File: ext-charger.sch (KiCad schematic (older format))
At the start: 61 parts

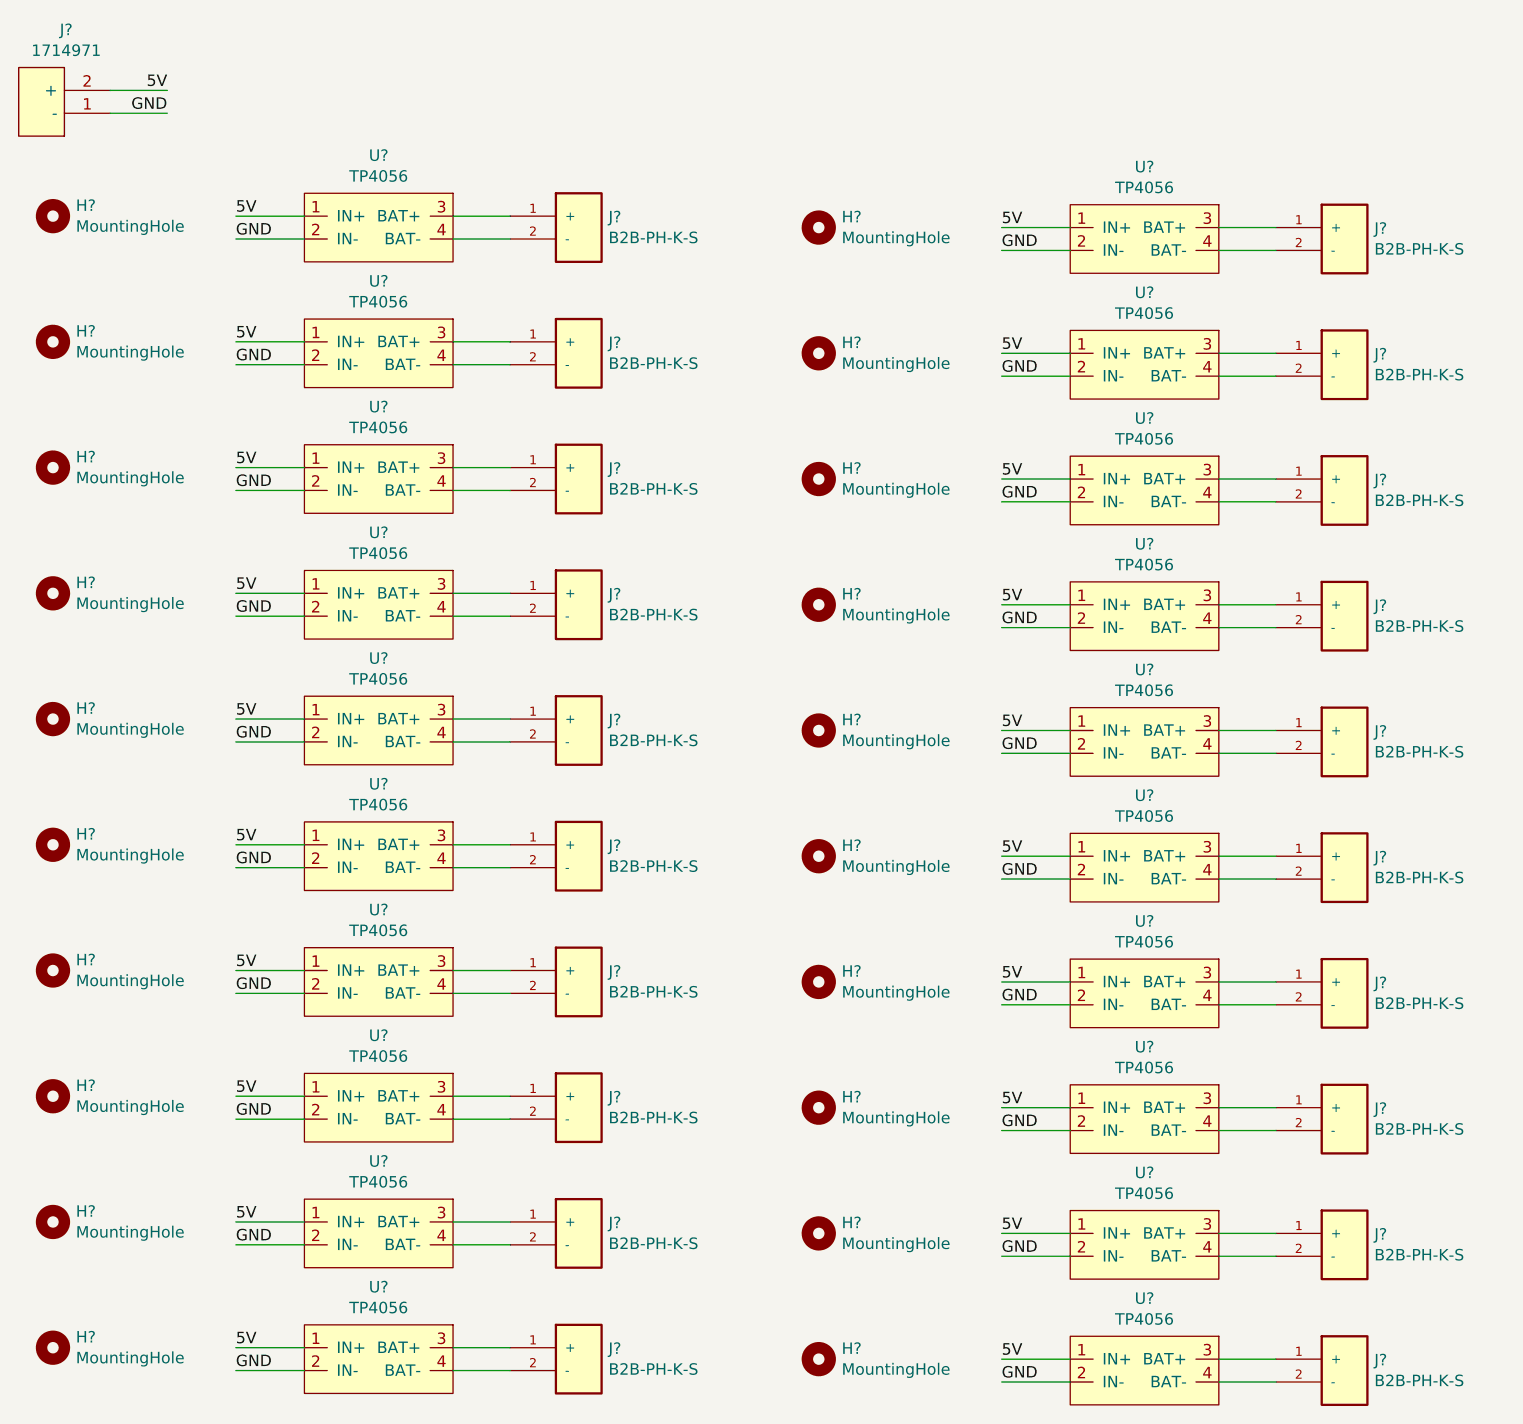
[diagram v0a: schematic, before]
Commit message: added filled zones
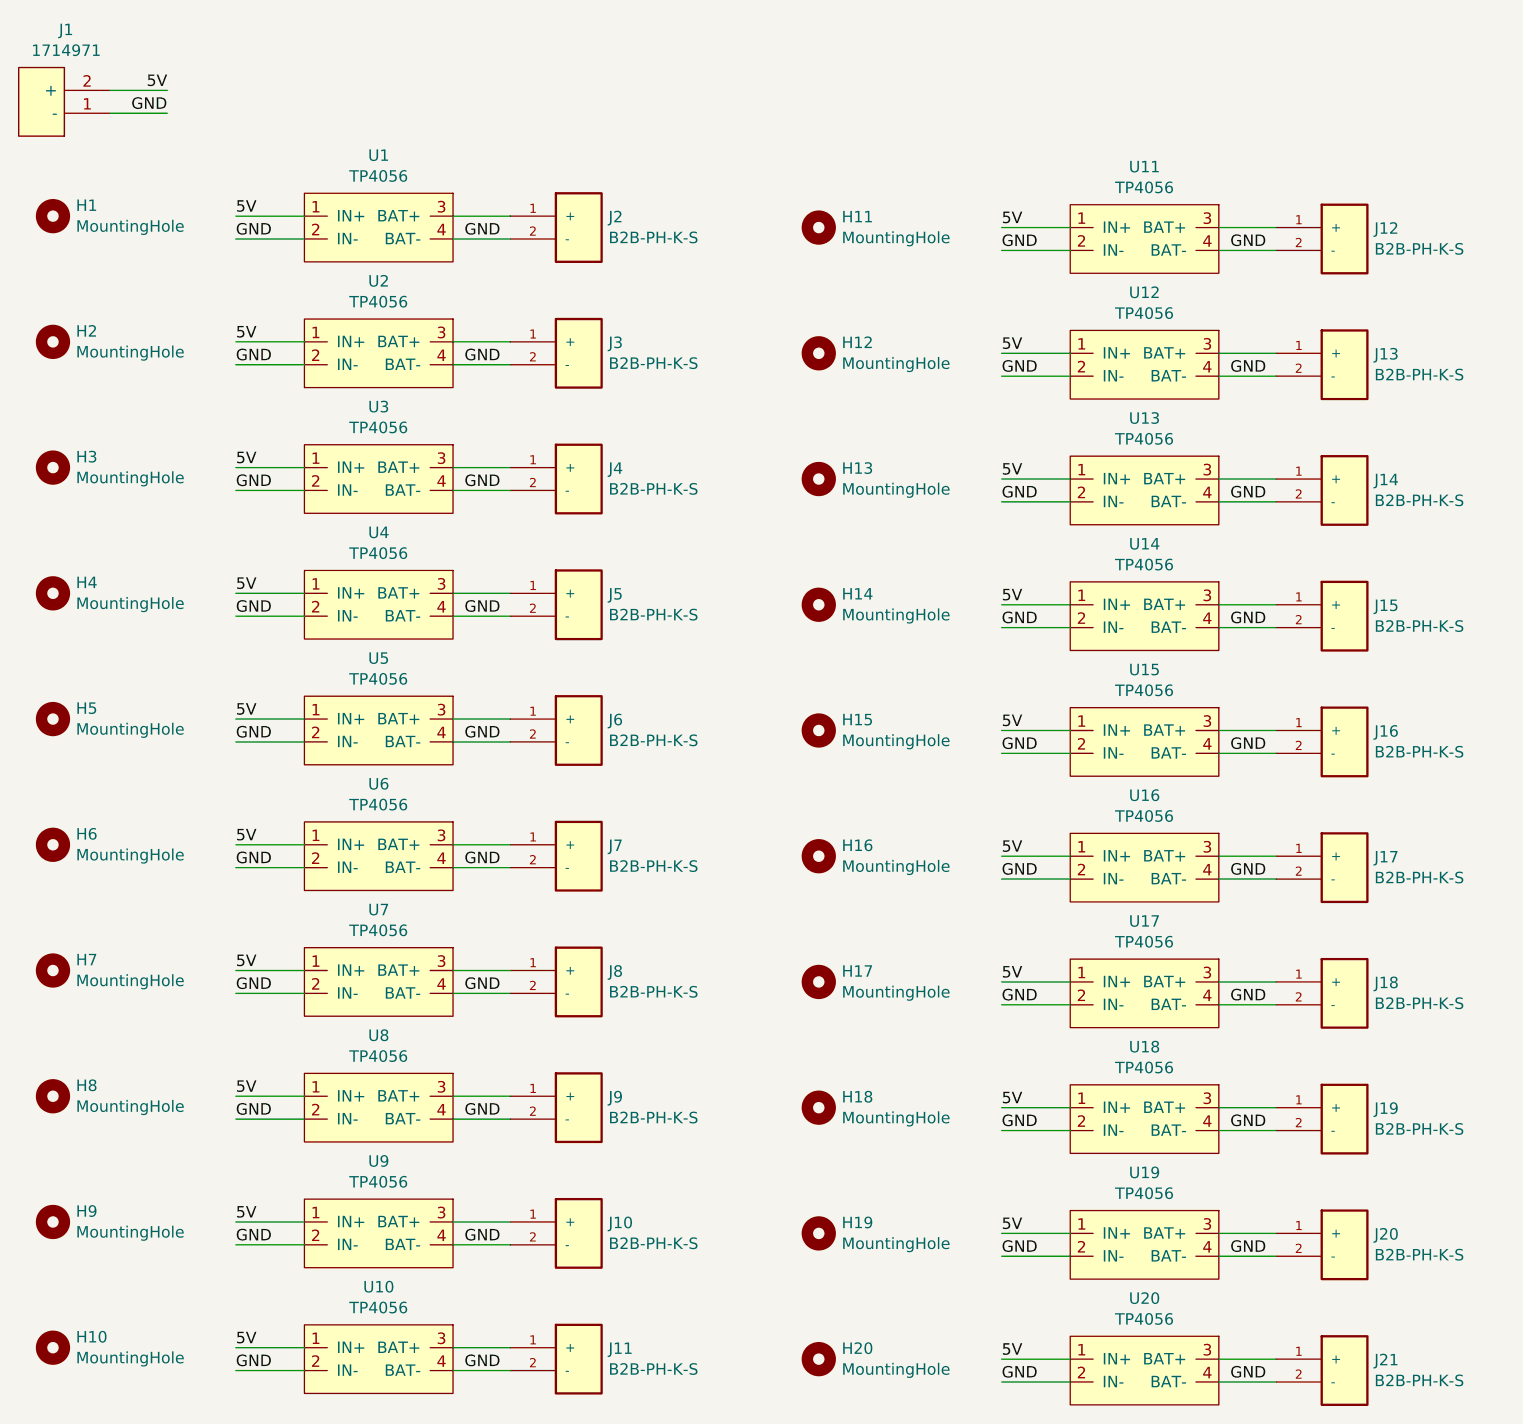
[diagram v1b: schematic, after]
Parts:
- gave numbers to parts that had none: 61
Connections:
- net GND: now also J10.2 (-), J11.2 (-), J12.2 (-), J13.2 (-), J14.2 (-), J15.2 (-), J16.2 (-), J17.2 (-), J18.2 (-), J19.2 (-), J2.2 (-), J20.2 (-), J21.2 (-), J3.2 (-), J4.2 (-), J5.2 (-), J6.2 (-), J7.2 (-), J8.2 (-), J9.2 (-), U1.4 (BAT-), U10.4 (BAT-), U11.4 (BAT-), U12.4 (BAT-), U13.4 (BAT-), U14.4 (BAT-), U15.4 (BAT-), U16.4 (BAT-), U17.4 (BAT-), U18.4 (BAT-), U19.4 (BAT-), U2.4 (BAT-), U20.4 (BAT-), U3.4 (BAT-), U4.4 (BAT-), U5.4 (BAT-), U6.4 (BAT-), U7.4 (BAT-), U8.4 (BAT-), U9.4 (BAT-)
